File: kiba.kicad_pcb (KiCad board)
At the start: 2 copper layers, 56.5 x 65 mm, 62 parts, among them IC1 SHT40-CD1B-R3, IC2 SGP40-D-R4, IC3 SGP40-D-R4, IC4 SGP40-D-R4, IC6 SGP40-D-R4, J1 Raspberry_Pi_2_3, Q1 2N7002NXAKR, U1 LM1117MP-3.3, U2 TCA9546APWR, U3 BMP581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

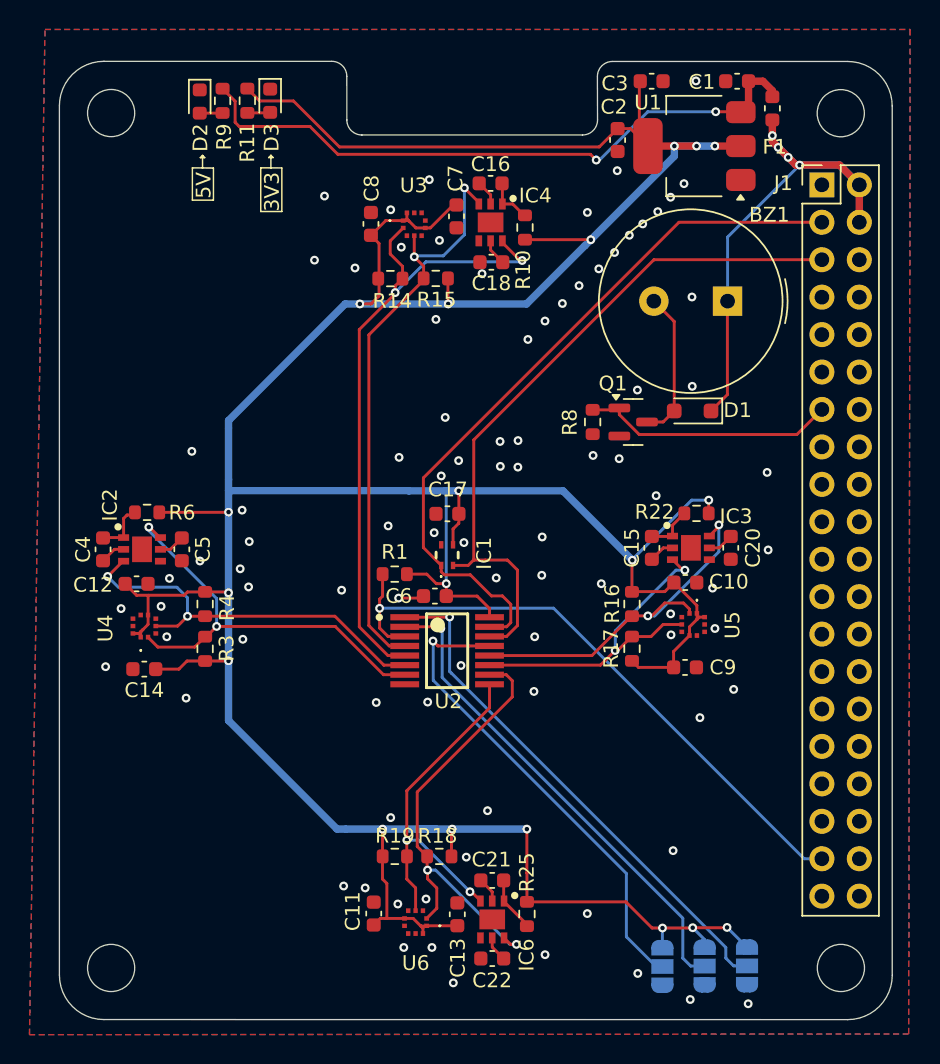
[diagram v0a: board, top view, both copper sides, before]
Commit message: fix: cps135b as new barometer
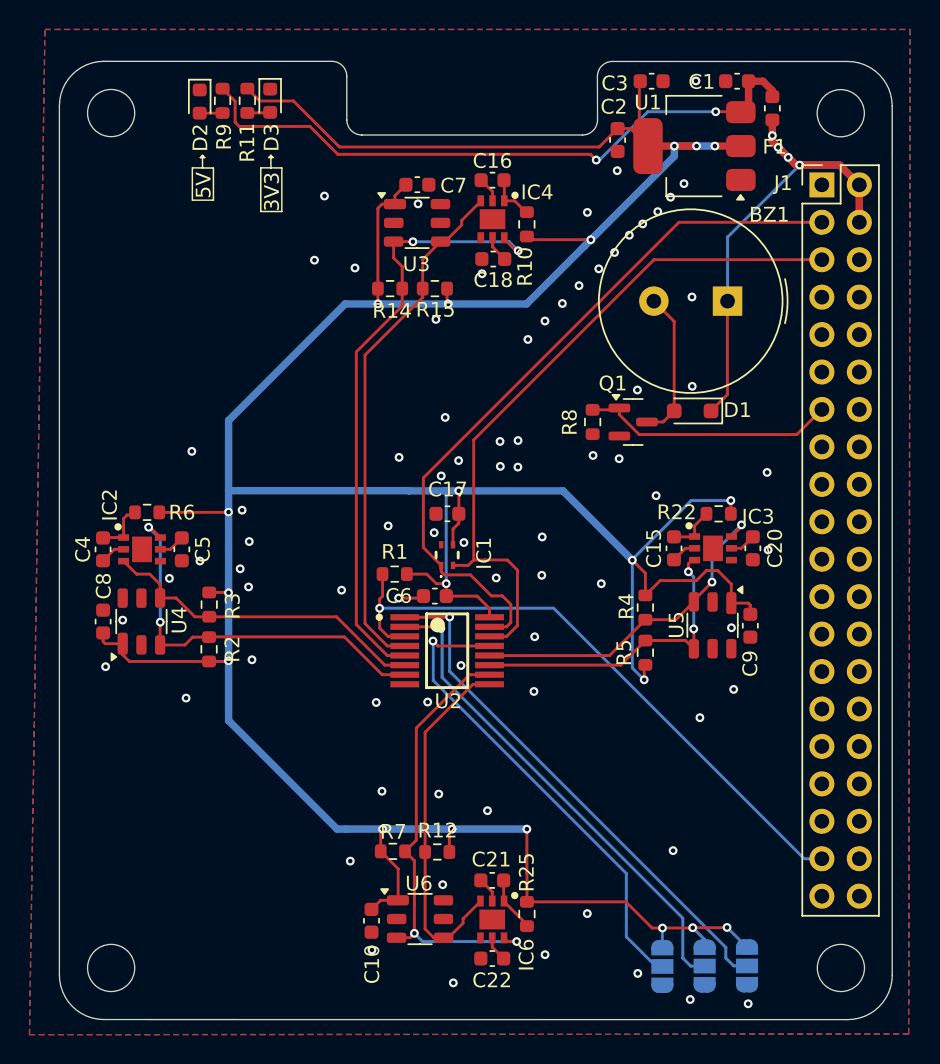
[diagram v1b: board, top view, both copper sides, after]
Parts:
- removed C11, C12, C13, C14: 100n, Capacitor_SMD:C_0603_1608Metric
- removed R16, R17, R18, R19: 2k2, Resistor_SMD:R_0603_1608Metric
- added R12: 2k2, Resistor_SMD:R_0603_1608Metric, F.Cu at (141.2, 123.3)
- added R2: 2k2, Resistor_SMD:R_0603_1608Metric, F.Cu at (125.7, 109.6)
- added R5: 2k2, Resistor_SMD:R_0603_1608Metric, F.Cu at (155.3, 109.8)
- added R7: 2k2, Resistor_SMD:R_0603_1608Metric, F.Cu at (138.2, 123.3)
- U3, U4, U5, U6: value BMP581 -> CPS135B; footprint Local:BMP581 -> smd6:smd6-4.5mm
- moved C8 32.5 mm to (118.5, 107.7)
- moved C10 31.3 mm to (136.8, 128.0), turned to -90 degrees
- moved R4 29.9 mm to (155.3, 106.8)
- moved C9 5.26 mm to (162.4, 108.0), turned to -90 degrees
- moved C7 3.42 mm to (139.9, 78.1), turned to 0 degrees
- moved R3 3.01 mm to (125.7, 106.6), turned to -90 degrees
- moved C15 1.50 mm to (157.3, 102.8)
- moved C20 1.50 mm to (162.6, 102.8)
- moved IC3 1.50 mm to (159.9, 102.8)
- moved R22 1.50 mm to (160.3, 100.4)
- moved U5 1.32 mm to (159.9, 108.0)
- moved R15 0.69 mm to (141.1, 85.1)
- moved R14 0.68 mm to (138.0, 85.1)
- moved U6 0.37 mm to (140.1, 127.9), turned to 0 degrees
- moved U4 0.37 mm to (121.1, 107.7)
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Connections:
- R3 pad 2: /Sensors/SCK_1 -> /Sensors/SDA_1
- R4 pad 2: /Sensors/SDA_1 -> /Sensors/SCK_2
- U3 pad 2: /Sensors/SCK_0 -> unconnected-(U3-N/A-Pad2)
- U3 pad 3: GND -> /Sensors/SCK_0
- U3 pad 5: GND -> unconnected-(U3-N/A-Pad5)
- U3 pad 6: +3V3 -> GND
- U4 pad 2: /Sensors/SCK_1 -> unconnected-(U4-N/A-Pad2)
- U4 pad 3: GND -> /Sensors/SCK_1
- U4 pad 5: GND -> unconnected-(U4-N/A-Pad5)
- U4 pad 6: +3V3 -> GND
- U5 pad 2: /Sensors/SCK_2 -> unconnected-(U5-N/A-Pad2)
- U5 pad 3: GND -> /Sensors/SCK_2
- U5 pad 5: GND -> unconnected-(U5-N/A-Pad5)
- U5 pad 6: +3V3 -> GND
- U6 pad 2: /Sensors/SCK_3 -> unconnected-(U6-N/A-Pad2)
- U6 pad 3: GND -> /Sensors/SCK_3
- U6 pad 5: GND -> unconnected-(U6-N/A-Pad5)
- U6 pad 6: +3V3 -> GND
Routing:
- net +3V3: track 279.5 -> 272.1 mm, vias 19 -> 20
- net /Sensors/SDA_1: track 27.3 -> 22.5 mm, vias 2 -> 0
- net /Sensors/SDA_0: track 40.0 -> 35.4 mm, vias 2 -> 0
- net /Sensors/SCK_0: track 44.3 -> 41.7 mm
- net /Sensors/SCK_1: track 29.4 -> 27.3 mm
- net /Sensors/SCK_2: track 25.0 -> 23.0 mm
- net /Sensors/SDA_2: track 23.1 -> 21.2 mm
- net /Sensors/SDA_3: track 24.6 -> 24.3 mm, vias 2 -> 0
- net GND: vias 88 -> 77

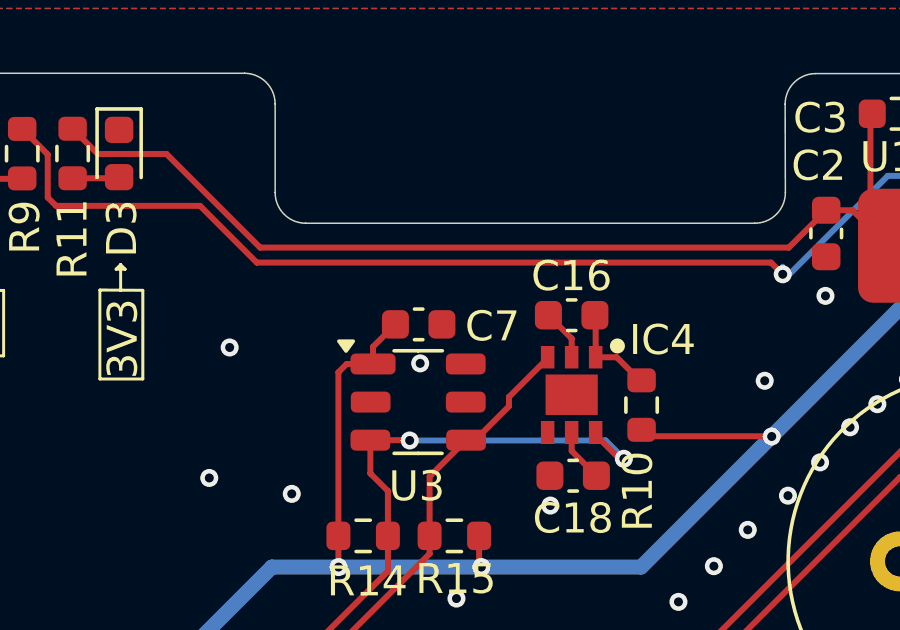
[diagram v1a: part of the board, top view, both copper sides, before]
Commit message: production files for jlcpcb, added passives for DNP sensors
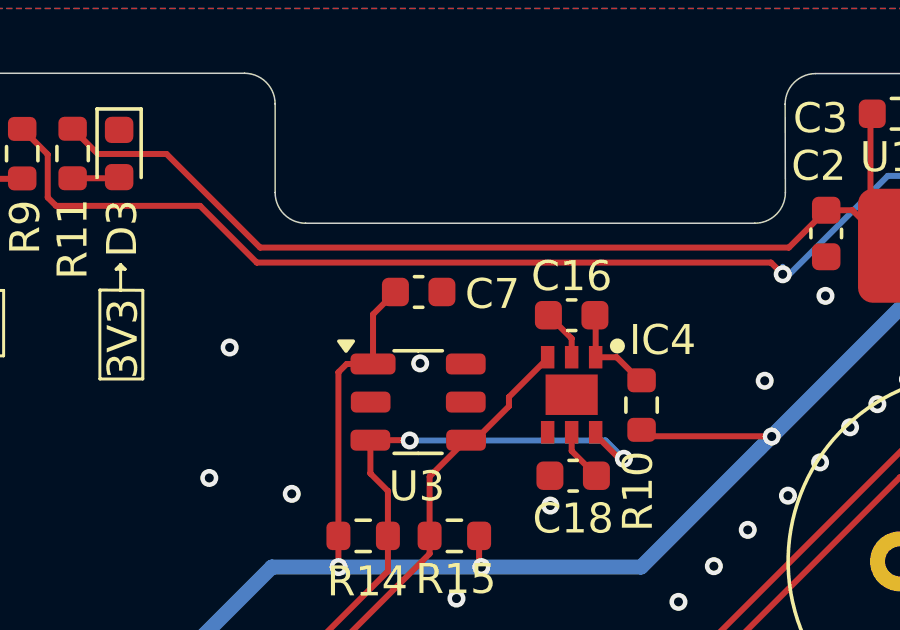
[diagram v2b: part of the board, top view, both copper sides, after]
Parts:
- moved C7 1.08 mm to (139.9, 77.0)
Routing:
- net +3V3: track 272.1 -> 273.2 mm
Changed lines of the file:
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@@
 		(sheetname "Sensors")
 		(sheetfile "sensors.kicad_sch")
-		(attr smd exclude_from_bom dnp)
+		(attr smd)
 		(fp_line
 			(start -0.237258 0.5225)
@@
 			)
 		)
-		(property "Datasheet" "https://www.bosch-sensortec.com/media/boschsensortec/downloads/datasheets/bst-bmp581-ds004.pdf"
+		(property "Datasheet" ""
 			(at 0 0 90)
 			(layer "F.Fab")
@@
 			)
 		)
-		(property "Mouser Part Number" "262-BMP581"
+		(property "Mouser Part Number" ""
 			(at 0 0 90)
 			(unlocked yes)
@@
 			)
 		)
-		(property "Mouser Price/Stock" "https://www.mouser.co.uk/ProductDetail/Bosch-Sensortec/BMP581?qs=Li%252BoUPsLEntPL9tlFmcgXg%3D%3D"
+		(property "Mouser Price/Stock" ""
 			(at 0 0 90)
 			(unlocked yes)
@@
 			)
 		)
-		(property "Manufacturer_Name" "BOSCH"
+		(property "Manufacturer_Name" ""
 			(at 0 0 90)
 			(unlocked yes)
@@
 			)
 		)
-		(property "Manufacturer_Part_Number" "BMP581"
+		(property "Manufacturer_Part_Number" ""
 			(at 0 0 90)
 			(unlocked yes)
@@
 			)
 		)
-		(property "LCSC" "C5362283"
+		(property "LCSC" "C491452"
 			(at 0 0 90)
 			(unlocked yes)
@@
 		(sheetname "Sensors")
 		(sheetfile "sensors.kicad_sch")
-		(attr smd exclude_from_bom dnp)
+		(attr smd)
 		(fp_line
 			(start -0.14058 0.51)
@@
 		(sheetname "Sensors")
 		(sheetfile "sensors.kicad_sch")
-		(attr smd exclude_from_bom dnp)
+		(attr smd)
 		(fp_line
 			(start -0.14058 0.51)
@@
 		(sheetname "Sensors")
 		(sheetfile "sensors.kicad_sch")
-		(attr smd exclude_from_bom dnp)
+		(attr smd)
 		(fp_line
 			(start -0.237258 0.5225)
@@
 		(sheetname "Root")
 		(sheetfile "kiba.kicad_sch")
-		(attr through_hole)
+		(attr through_hole exclude_from_bom dnp)
 		(fp_arc
 			(start -3.9 1.499999)
@@
 		(sheetname "Sensors")
 		(sheetfile "sensors.kicad_sch")
-		(attr smd exclude_from_bom dnp)
+		(attr smd)
 		(fp_line
 			(start -0.237258 0.5225)
@@
 		(tags "resistor")
 		(property "Reference" "R12"
-			(at -0.02 1.45 360)
+			(at -0.02 1.45 0)
 			(layer "F.SilkS")
 			(effects
@@
 		)
 		(property "Value" "2k2"
-			(at 0 1.43 360)
+			(at 0 1.43 0)
 			(layer "F.Fab")
 			(effects
@@
 		)
 		(fp_text user "${REFERENCE}"
-			(at 0 0 360)
+			(at 0 0 0)
 			(layer "F.Fab")
 			(effects
@@
 			)
 		)
-		(property "Datasheet" "https://www.bosch-sensortec.com/media/boschsensortec/downloads/datasheets/bst-bmp581-ds004.pdf"
+		(property "Datasheet" ""
 			(at 0 0 -90)
 			(layer "F.Fab")
@@
 			)
 		)
-		(property "Mouser Part Number" "262-BMP581"
+		(property "Mouser Part Number" ""
 			(at 0 0 -90)
 			(unlocked yes)
@@
 			)
 		)
-		(property "Mouser Price/Stock" "https://www.mouser.co.uk/ProductDetail/Bosch-Sensortec/BMP581?qs=Li%252BoUPsLEntPL9tlFmcgXg%3D%3D"
+		(property "Mouser Price/Stock" ""
 			(at 0 0 -90)
 			(unlocked yes)
@@
 			)
 		)
-		(property "Manufacturer_Name" "BOSCH"
+		(property "Manufacturer_Name" ""
 			(at 0 0 -90)
 			(unlocked yes)
@@
 			)
 		)
-		(property "Manufacturer_Part_Number" "BMP581"
+		(property "Manufacturer_Part_Number" ""
 			(at 0 0 -90)
 			(unlocked yes)
@@
 			)
 		)
-		(property "LCSC" "C5362283"
+		(property "LCSC" "C491452"
 			(at 0 0 -90)
 			(unlocked yes)
@@
 		(tags "TSOT TO_SOT_SMD")
 		(property "Reference" "U6"
-			(at -0.08 -2.4 360)
+			(at -0.08 -2.4 0)
 			(layer "F.SilkS")
 			(effects
@@
 		)
 		(property "Value" "CPS135B"
-			(at 0 2.4 360)
+			(at 0 2.4 0)
 			(layer "F.Fab")
 			(effects
@@
 		)
 		(property "Footprint" "smd6:smd6-4.5mm"
-			(at 0 0 360)
+			(at 0 0 0)
 			(layer "F.Fab")
 			(hide yes)
@@
 			)
 		)
-		(property "Datasheet" "https://www.bosch-sensortec.com/media/boschsensortec/downloads/datasheets/bst-bmp581-ds004.pdf"
-			(at 0 0 360)
+		(property "Datasheet" ""
+			(at 0 0 0)
 			(layer "F.Fab")
 			(hide yes)
@@
 		)
 		(property "Description" "Pressure Sensor 4.35PSI ~ 18.13PSI (30kPa ~ 125kPa) Absolute 10-WFLGA"
-			(at 0 0 360)
+			(at 0 0 0)
 			(layer "F.Fab")
 			(hide yes)
@@
 			)
 		)
-		(property "Mouser Part Number" "262-BMP581"
-			(at 0 0 0)
-			(unlocked yes)
-			(layer "F.Fab")
-			(hide yes)
-			(effects
-				(font
-					(size 1 1)
-					(thickness 0.15)
-				)
-			)
-		)
-		(property "Mouser Price/Stock" "https://www.mouser.co.uk/ProductDetail/Bosch-Sensortec/BMP581?qs=Li%252BoUPsLEntPL9tlFmcgXg%3D%3D"
-			(at 0 0 0)
-			(unlocked yes)
-			(layer "F.Fab")
-			(hide yes)
-			(effects
-				(font
-					(size 1 1)
-					(thickness 0.15)
-				)
-			)
-		)
-		(property "Manufacturer_Name" "BOSCH"
-			(at 0 0 0)
-			(unlocked yes)
-			(layer "F.Fab")
-			(hide yes)
-			(effects
-				(font
-					(size 1 1)
-					(thickness 0.15)
-				)
-			)
-		)
-		(property "Manufacturer_Part_Number" "BMP581"
-			(at 0 0 0)
-			(unlocked yes)
-			(layer "F.Fab")
-			(hide yes)
-			(effects
-				(font
-					(size 1 1)
-					(thickness 0.15)
-				)
-			)
-		)
-		(property "LCSC" "C5362283"
+		(property "LCSC" "C491452"
 			(at 0 0 0)
 			(unlocked yes)
@@
 		)
 		(fp_text user "${REFERENCE}"
-			(at 0 0 360)
+			(at 0 0 0)
 			(layer "F.Fab")
 			(effects
@@
 		(sheetname "Sensors")
 		(sheetfile "sensors.kicad_sch")
-		(attr smd exclude_from_bom dnp)
+		(attr smd)
 		(fp_line
 			(start -0.14058 0.51)
@@
 		(sheetname "Sensors")
 		(sheetfile "sensors.kicad_sch")
-		(attr smd exclude_from_bom dnp)
+		(attr smd)
 		(fp_line
 			(start -0.237258 -0.5225)
@@
 		(sheetname "Sensors")
 		(sheetfile "sensors.kicad_sch")
-		(attr smd exclude_from_bom dnp)
+		(attr smd)
 		(fp_line
 			(start -0.237258 0.5225)
@@
 		(sheetname "Sensors")
 		(sheetfile "sensors.kicad_sch")
-		(attr smd exclude_from_bom dnp)
+		(attr smd)
 		(fp_line
 			(start -0.237258 -0.5225)
@@
 		(sheetname "Sensors")
 		(sheetfile "sensors.kicad_sch")
-		(attr smd exclude_from_bom dnp)
+		(attr smd)
 		(fp_line
 			(start -0.14058 0.51)
@@
 		(sheetname "Root")
 		(sheetfile "kiba.kicad_sch")
-		(attr through_hole)
+		(attr through_hole exclude_from_bom dnp)
 		(fp_line
 			(start -1.33 -1.32)
@@
 		(tags "resistor")
 		(property "Reference" "R7"
-			(at 0.03 -1.32 360)
+			(at 0.03 -1.32 0)
 			(layer "F.SilkS")
 			(effects
@@
 		)
 		(property "Value" "2k2"
-			(at 0 1.43 360)
+			(at 0 1.43 0)
 			(layer "F.Fab")
 			(effects
@@
 		)
 		(fp_text user "${REFERENCE}"
-			(at 0 0 360)
+			(at 0 0 0)
 			(layer "F.Fab")
 			(effects
@@
 		(sheetname "Sensors")
 		(sheetfile "sensors.kicad_sch")
-		(attr smd exclude_from_bom dnp)
+		(attr smd)
 		(fp_line
 			(start -0.14058 0.51)
@@
 	(footprint "Capacitor_SMD:C_0603_1608Metric"
 		(layer "F.Cu")
-		(at 139.86 78.08)
+		(at 139.86 77)
 		(descr "Capacitor SMD 0603 (1608 Metric), square (rectangular) end terminal, IPC_7351 nominal, (Body size source: IPC-SM-782 page 76, https://www.pcb-3d.com/wordpress/wp-content/uploads/ipc-sm-782a_amendment_1_and_2.pdf), generated with kicad-footprint-generator")
 		(tags "capacitor")
 		(property "Reference" "C7"
-			(at 2.46 0.07 360)
+			(at 2.46 0.07 0)
 			(layer "F.SilkS")
 			(effects
@@
 		)
 		(property "Value" "100n"
-			(at 0 1.43 360)
+			(at 0 1.43 0)
 			(layer "F.Fab")
 			(effects
@@
 		)
 		(fp_text user "${REFERENCE}"
-			(at 0 0 360)
+			(at 0 0 0)
 			(layer "F.Fab")
 			(effects
@@
 			)
 		)
-		(property "Datasheet" "https://www.bosch-sensortec.com/media/boschsensortec/downloads/datasheets/bst-bmp581-ds004.pdf"
+		(property "Datasheet" ""
 			(at 0 0 0)
 			(layer "F.Fab")
@@
 			)
 		)
-		(property "Mouser Part Number" "262-BMP581"
+		(property "Mouser Part Number" ""
 			(at 0 0 0)
 			(unlocked yes)
@@
 			)
 		)
-		(property "Mouser Price/Stock" "https://www.mouser.co.uk/ProductDetail/Bosch-Sensortec/BMP581?qs=Li%252BoUPsLEntPL9tlFmcgXg%3D%3D"
+		(property "Mouser Price/Stock" ""
 			(at 0 0 0)
 			(unlocked yes)
@@
 			)
 		)
-		(property "Manufacturer_Name" "BOSCH"
+		(property "Manufacturer_Name" ""
 			(at 0 0 0)
 			(unlocked yes)
@@
 			)
 		)
-		(property "Manufacturer_Part_Number" "BMP581"
+		(property "Manufacturer_Part_Number" ""
 			(at 0 0 0)
 			(unlocked yes)
@@
 			)
 		)
-		(property "LCSC" "C5362283"
+		(property "LCSC" "C491452"
 			(at 0 0 0)
 			(unlocked yes)
@@
 		(sheetname "Sensors")
 		(sheetfile "sensors.kicad_sch")
-		(attr smd exclude_from_bom dnp)
+		(attr smd)
 		(fp_line
 			(start -0.14058 -0.51)
@@
 	)
 	(segment
+		(start 138.33875 77.74625)
+		(end 139.085 77)
+		(width 0.2)
+		(layer "F.Cu")
+		(net 7)
+	)
+	(segment
 		(start 137.185 86.165)
 		(end 137.19 86.17)
@@
 	)
 	(segment
-		(start 138.33875 79.4)
-		(end 138.33875 78.82625)
-		(width 0.2)
-		(layer "F.Cu")
-		(net 7)
-	)
-	(segment
 		(start 118.54 109.08)
 		(end 118.68125 109.22125)
@@
 	)
 	(segment
+		(start 138.33875 79.4)
+		(end 138.33875 77.74625)
+		(width 0.2)
+		(layer "F.Cu")
+		(net 7)
+	)
+	(segment
 		(start 141.825384 105.99)
 		(end 143.91 105.99)
@@
 	)
 	(segment
-		(start 138.33875 78.82625)
-		(end 139.085 78.08)
-		(width 0.2)
-		(layer "F.Cu")
-		(net 7)
-	)
-	(segment
 		(start 125.74 105.745)
 		(end 127.025 105.745)
@@
 		(net 3)
 		(net_name "GND")
-		(layers "F.Cu" "B.Cu")
+		(layers "F&B.Cu")
 		(hatch edge 0.5)
 		(connect_pads yes
